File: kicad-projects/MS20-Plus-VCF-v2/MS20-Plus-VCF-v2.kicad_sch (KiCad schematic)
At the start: 78 parts

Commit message: Minor cleanups
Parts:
- added R? (x2): R, symbol Device:R
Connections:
- net GNDA: now also R?.2, R?.2
- net HP_In_P: now also R?.1
- net LP_In_P: now also R?.1
- net SC_HpG1_P: now also D?.1 (K), D?.2 (A); no longer D?.1 (K), D?.2 (A)
- net SC_HpG2_P: now also D?.1 (K), D?.2 (A); no longer D?.1 (K), D?.2 (A)
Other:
- moved on the sheet: C?, D?, J?, R?, RV?, SW?, U?A, U?B, U?C, U?D

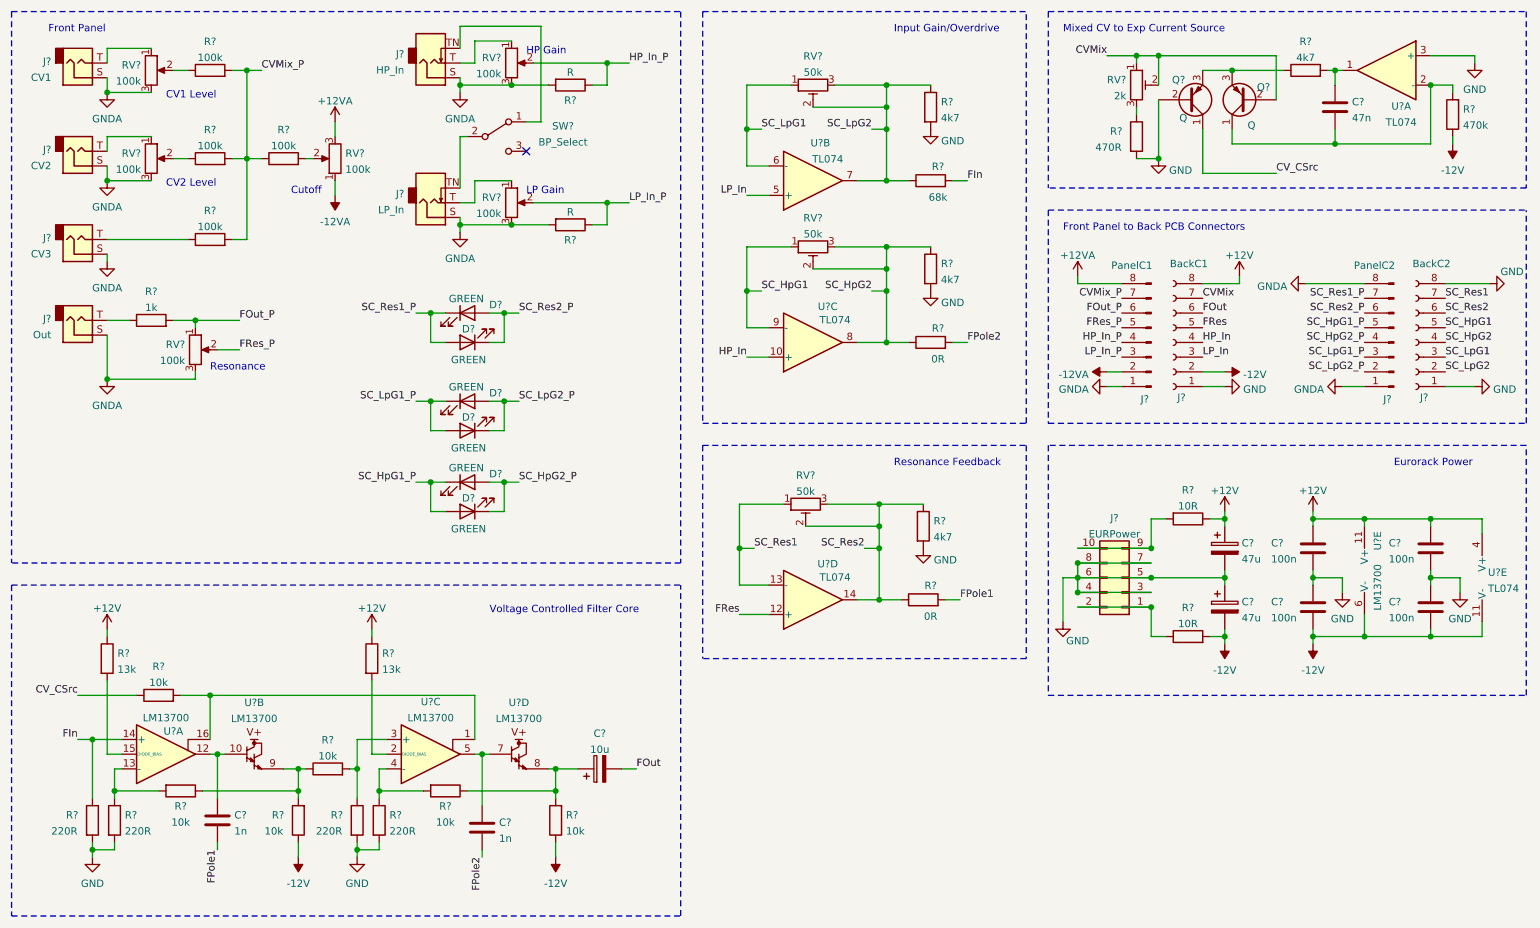
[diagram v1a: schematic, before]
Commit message: Added PCB for MS20 filter, and BOM for VCO
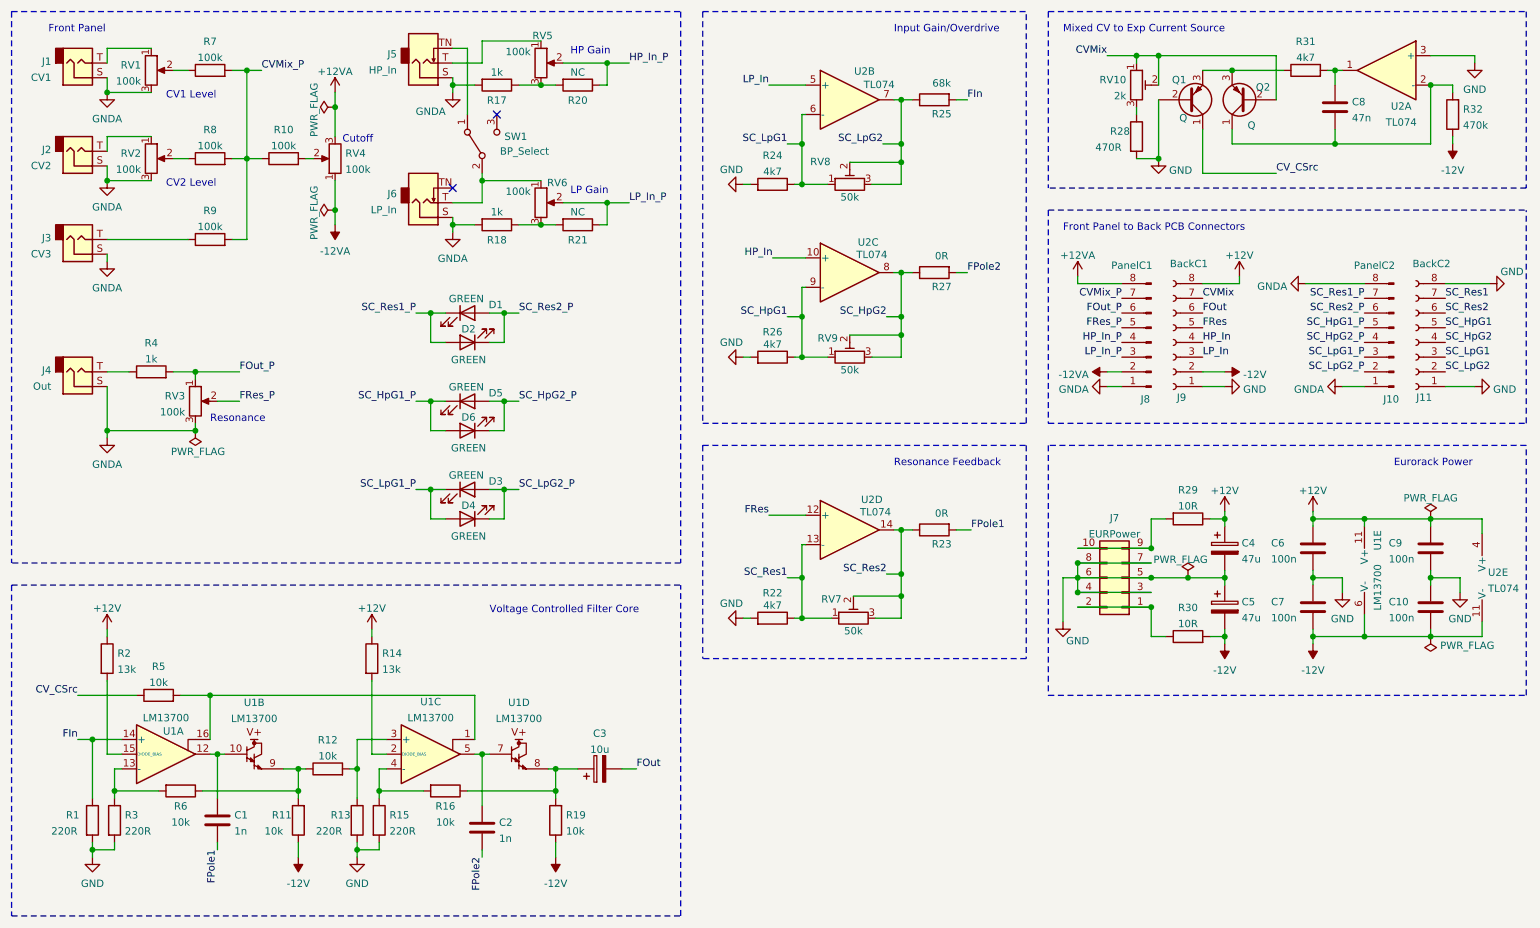
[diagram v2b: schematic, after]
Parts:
- added R17, R18: 1k, Resistor_THT:R_Axial_DIN0207_L6.3mm_D2.5mm_P7.62mm_Horizontal, symbol Device:R
- C1, C10, C2, C6, C7, C8, C9: renamed from C?; footprint (none) -> Capacitor_THT:C_Rect_L7.0mm_W3.5mm_P5.00mm
- C3: renamed from C?; footprint (none) -> Capacitor_THT:CP_Radial_D5.0mm_P2.50mm
- C4, C5: renamed from C?; footprint (none) -> Capacitor_THT:CP_Radial_D6.3mm_P2.50mm
- D1, D2, D3, D4, D5, D6: renamed from D?; footprint (none) -> LED_THT:LED_D3.0mm
- J1, J2, J3, J4, J5, J6: renamed from J?; footprint (none) -> Connector_Audio:Jack_3.5mm_QingPu_WQP-PJ398SM_Vertical_CircularHoles
- J10, J8: renamed from J?; footprint (none) -> Connector_PinHeader_2.54mm:PinHeader_1x08_P2.54mm_Vertical
- J11, J9: renamed from J?; footprint (none) -> Connector_PinSocket_2.54mm:PinSocket_1x08_P2.54mm_Vertical
- J7: renamed from J?; footprint (none) -> Connector_IDC:IDC-Header_2x05_P2.54mm_Vertical
- Q1, Q2: renamed from Q?; footprint (none) -> Package_TO_SOT_THT:TO-92_Inline
- R1, R10, R11, R12, R13, R14, R15, R16, R19, R2, R22, R23, R24, R25, R26, R27, R28, R29, R3, R30, R31, R32, R4, R5, R6, R7, R8, R9: renamed from R?; footprint (none) -> Resistor_THT:R_Axial_DIN0207_L6.3mm_D2.5mm_P7.62mm_Horizontal
- R20, R21: renamed from R?; value R -> NC; footprint (none) -> Resistor_THT:R_Axial_DIN0207_L6.3mm_D2.5mm_P7.62mm_Horizontal
- RV1, RV2, RV3, RV4, RV5, RV6: renamed from RV?; footprint (none) -> Potentiometer_THT:Potentiometer_Alpha_RD901F-40-00D_Single_Vertical
- RV10, RV7, RV8, RV9: renamed from RV?; footprint (none) -> Potentiometer_THT:Potentiometer_Bourns_3296W_Vertical
- SW1: renamed from SW?; footprint (none) -> Switches:5mm_rocker_toggle_switch
- U1: renamed from U?; footprint (none) -> Package_DIP:DIP-16_W7.62mm
- U2: renamed from U?; footprint (none) -> Package_DIP:DIP-14_W7.62mm
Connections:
- net GNDA: now also R17.2, R18.2; no longer R20.2, R21.2, RV5.3, RV6.3
- net SC_HpG1: now also R26.1
- net SC_HpG2: no longer R26.1
- net SC_LpG1: now also R24.1
- net SC_LpG2: no longer R24.1
- net SC_Res1: now also R22.1
- net SC_Res2: no longer R22.1
- net at J6.T, RV6.1: now also SW1.2 (B)
- net at J6.TN: no longer SW1.2 (B)
- new net: R17.1, R20.2, RV5.3
- new net: R18.1, R21.2, RV6.3
- no-connect marks 1 -> 2
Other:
- company: (none) -> The Synth Project
- title: (none) -> MS20 Plus - Voltage Controlled Filter
- moved on the sheet: D3, D4, D5, D6, J4, J5, J6, R20, R21, R22, R23, R24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

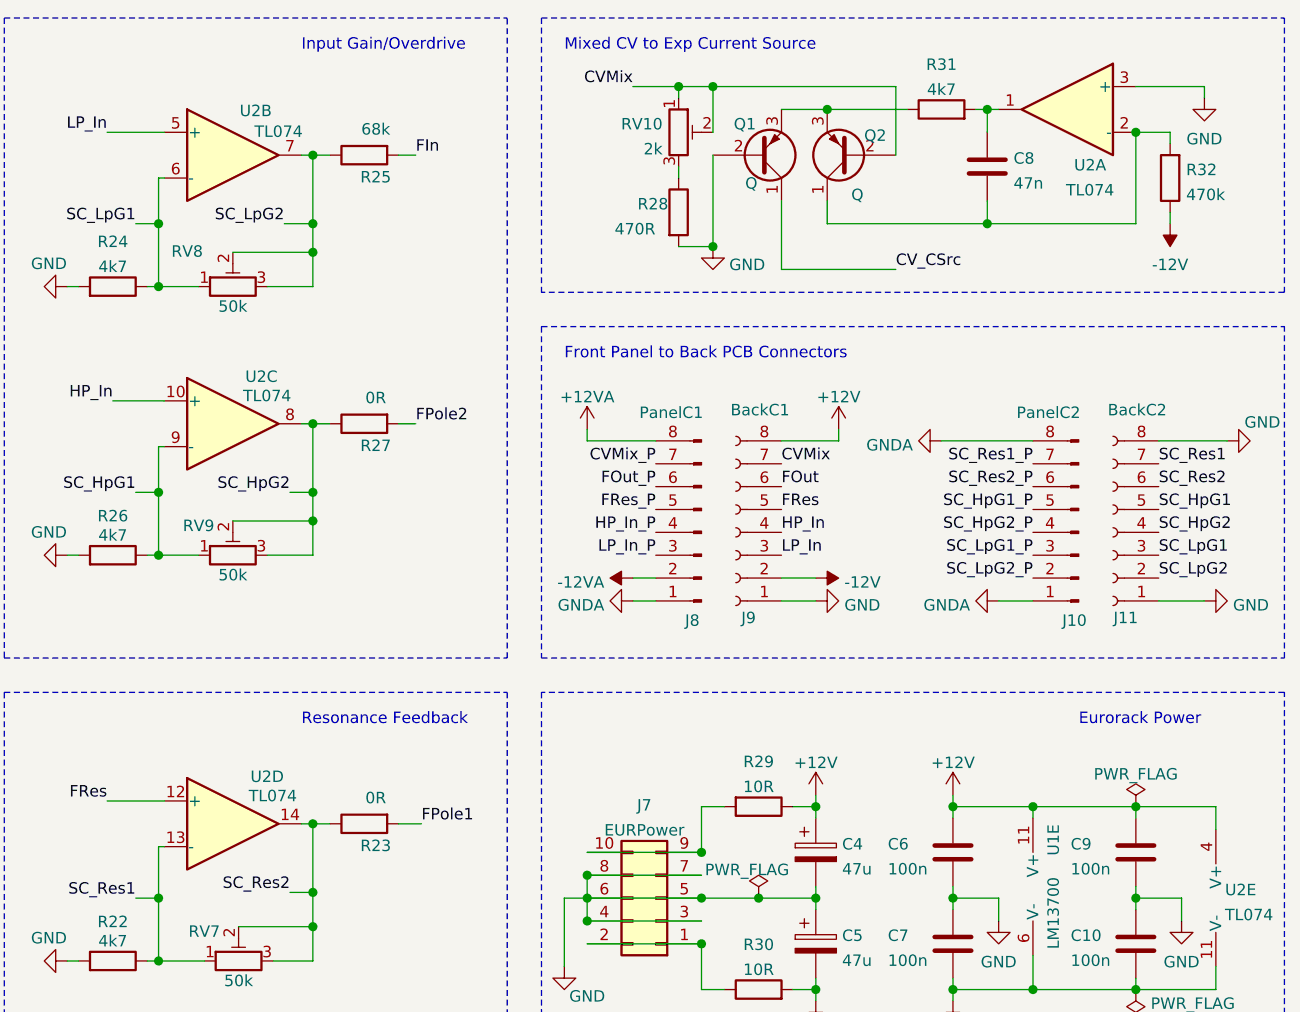
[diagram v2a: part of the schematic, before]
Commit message: More work on the MS20 VCF. Closing in on a final placement.
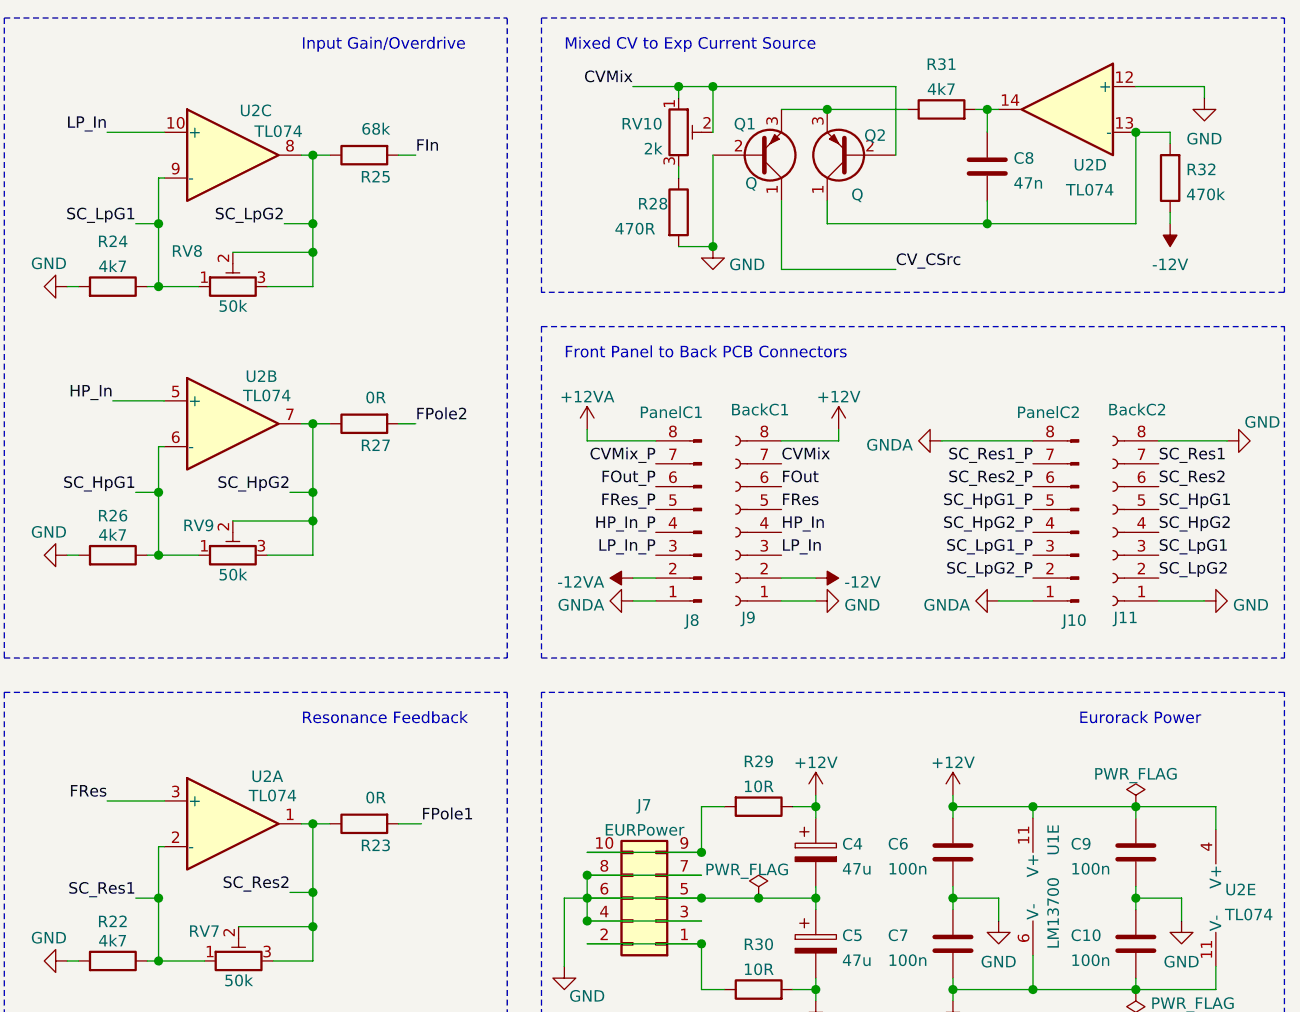
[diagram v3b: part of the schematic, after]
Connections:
- net FRes: now also U2.3 (+); no longer U2.12 (+)
- net GND: now also U2.12 (+); no longer U2.3 (+)
- net HP_In: now also U2.5 (+); no longer U2.10 (+)
- net LP_In: now also U2.10 (+); no longer U2.5 (+)
- net SC_HpG1: now also U2.6 (-); no longer U2.9 (-)
- net SC_HpG2: now also U2.7; no longer U2.8
- net SC_LpG1: now also U2.9 (-); no longer U2.6 (-)
- net SC_LpG2: now also U2.8; no longer U2.7
- net SC_Res1: now also U2.2 (-); no longer U2.13 (-)
- net SC_Res2: now also U2.1; no longer U2.14
- net at C8.2, Q2.1 (C), R32.2: now also U2.13 (-); no longer U2.2 (-)
- net at C8.1, R31.2: now also U2.14; no longer U2.1
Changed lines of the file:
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@@
     (pin "5")
   )
-  (symbol (lib_id "Amplifier_Operational:TL074") (at 161.29 43.18 0) (unit 2)
+  (symbol (lib_id "Amplifier_Operational:TL074") (at 161.29 43.18 0) (unit 3)
     (in_bom yes) (on_board yes)
     (property "Reference" "U2" (id 0) (at 163.83 38.2566 0))
@@
       (effects (font (size 1.27 1.27)) hide)
     )
-    (pin "5")
-    (pin "6")
-    (pin "7")
-  )
-  (symbol (lib_id "Amplifier_Operational:TL074") (at 161.29 73.025 0) (unit 3)
+    (pin "10")
+    (pin "8")
+    (pin "9")
+  )
+  (symbol (lib_id "Amplifier_Operational:TL074") (at 161.29 73.025 0) (unit 2)
     (in_bom yes) (on_board yes)
     (property "Reference" "U2" (id 0) (at 164.465 67.7884 0))
@@
       (effects (font (size 1.27 1.27)) hide)
     )
-    (pin "10")
-    (pin "8")
-    (pin "9")
-  )
-  (symbol (lib_id "Amplifier_Operational:TL074") (at 161.29 117.475 0) (unit 4)
+    (pin "5")
+    (pin "6")
+    (pin "7")
+  )
+  (symbol (lib_id "Amplifier_Operational:TL074") (at 161.29 117.475 0) (unit 1)
     (in_bom yes) (on_board yes)
     (property "Reference" "U2" (id 0) (at 165.1 112.2384 0))
@@
       (effects (font (size 1.27 1.27)) hide)
     )
-    (pin "12")
-    (pin "13")
-    (pin "14")
-  )
-  (symbol (lib_id "Amplifier_Operational:TL074") (at 254 38.1 0) (mirror y) (unit 1)
+    (pin "1")
+    (pin "2")
+    (pin "3")
+  )
+  (symbol (lib_id "Amplifier_Operational:TL074") (at 254 38.1 0) (mirror y) (unit 4)
     (in_bom yes) (on_board yes)
     (property "Reference" "U2" (id 0) (at 256.54 44.2934 0))
@@
       (effects (font (size 1.27 1.27)) hide)
     )
-    (pin "1")
-    (pin "2")
-    (pin "3")
+    (pin "12")
+    (pin "13")
+    (pin "14")
   )
   (symbol (lib_id "Connector_Generic:Conn_02x05_Odd_Even") (at 208.28 125.73 180) (unit 1)
@@
       (reference "U1") (unit 5) (value "LM13700") (footprint "Package_DIP:DIP-16_W7.62mm")
     )
+    (path "/5af32911-d340-491b-b73d-ce472113d571"
+      (reference "U2") (unit 1) (value "TL074") (footprint "Package_DIP:DIP-14_W7.62mm")
+    )
+    (path "/f83059ad-fef0-4da8-b6f0-c9df7fbd3a40"
+      (reference "U2") (unit 2) (value "TL074") (footprint "Package_DIP:DIP-14_W7.62mm")
+    )
+    (path "/8f0ce76b-f008-42b4-89fc-cf393fcf26b6"
+      (reference "U2") (unit 3) (value "TL074") (footprint "Package_DIP:DIP-14_W7.62mm")
+    )
     (path "/a6ded9fe-2ea8-4a24-926e-e1af8a7cae28"
-      (reference "U2") (unit 1) (value "TL074") (footprint "Package_DIP:DIP-14_W7.62mm")
-    )
-    (path "/8f0ce76b-f008-42b4-89fc-cf393fcf26b6"
-      (reference "U2") (unit 2) (value "TL074") (footprint "Package_DIP:DIP-14_W7.62mm")
-    )
-    (path "/f83059ad-fef0-4da8-b6f0-c9df7fbd3a40"
-      (reference "U2") (unit 3) (value "TL074") (footprint "Package_DIP:DIP-14_W7.62mm")
-    )
-    (path "/5af32911-d340-491b-b73d-ce472113d571"
       (reference "U2") (unit 4) (value "TL074") (footprint "Package_DIP:DIP-14_W7.62mm")
     )

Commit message: Tidied up
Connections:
- net +12V: now also J9.2 (Pin_2); no longer J9.8 (Pin_8)
- net +12VA: now also J8.2 (Pin_2); no longer J8.8 (Pin_8)
- net -12V: now also J9.8 (Pin_8); no longer J9.2 (Pin_2)
- net -12VA: now also J8.8 (Pin_8); no longer J8.2 (Pin_2)
- net CVMix: now also J9.3 (Pin_3); no longer J9.7 (Pin_7)
- net CVMix_P: now also J8.3 (Pin_3); no longer J8.7 (Pin_7)
- net FOut: now also J9.1 (Pin_1); no longer J9.6 (Pin_6)
- net FOut_P: now also J8.1 (Pin_1); no longer J8.6 (Pin_6)
- net FRes: now also U2.5 (+); no longer U2.3 (+)
- net GND: now also J9.6 (Pin_6); no longer J9.1 (Pin_1)
- net GNDA: now also J8.6 (Pin_6); no longer J8.1 (Pin_1)
- net HP_In: now also U2.3 (+); no longer U2.5 (+)
- net LP_In: now also J9.7 (Pin_7); no longer J9.3 (Pin_3)
- net LP_In_P: now also J8.7 (Pin_7); no longer J8.3 (Pin_3)
- net SC_HpG1: now also U2.2 (-); no longer U2.6 (-)
- net SC_HpG2: now also U2.1; no longer U2.7
- net SC_LpG1: now also J11.6 (Pin_6); no longer J11.3 (Pin_3)
- net SC_LpG1_P: now also J10.6 (Pin_6); no longer J10.3 (Pin_3)
- net SC_LpG2: now also J11.7 (Pin_7); no longer J11.2 (Pin_2)
- net SC_LpG2_P: now also J10.7 (Pin_7); no longer J10.2 (Pin_2)
- net SC_Res1: now also J11.2 (Pin_2), U2.6 (-); no longer J11.7 (Pin_7), U2.2 (-)
- net SC_Res1_P: now also J10.2 (Pin_2); no longer J10.7 (Pin_7)
- net SC_Res2: now also J11.3 (Pin_3), U2.7; no longer J11.6 (Pin_6), U2.1
- net SC_Res2_P: now also J10.3 (Pin_3); no longer J10.6 (Pin_6)
